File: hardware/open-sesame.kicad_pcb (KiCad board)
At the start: 2 copper layers, 72.2 x 45 mm, 9 parts, among them J1 Conn_01x10, J3 Barrel_Jack_Switch, J4 Conn_01x06_Socket

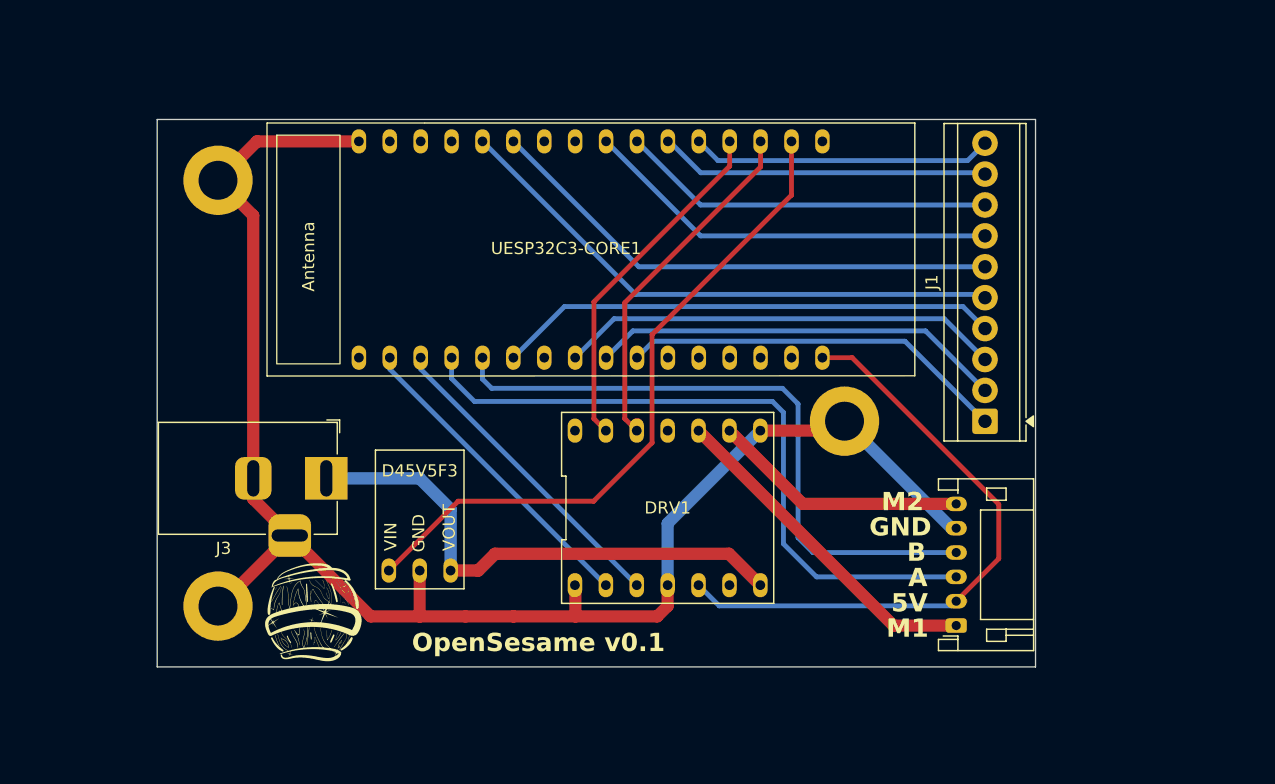
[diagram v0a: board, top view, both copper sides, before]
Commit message: Updated 3V & GND to terminal block
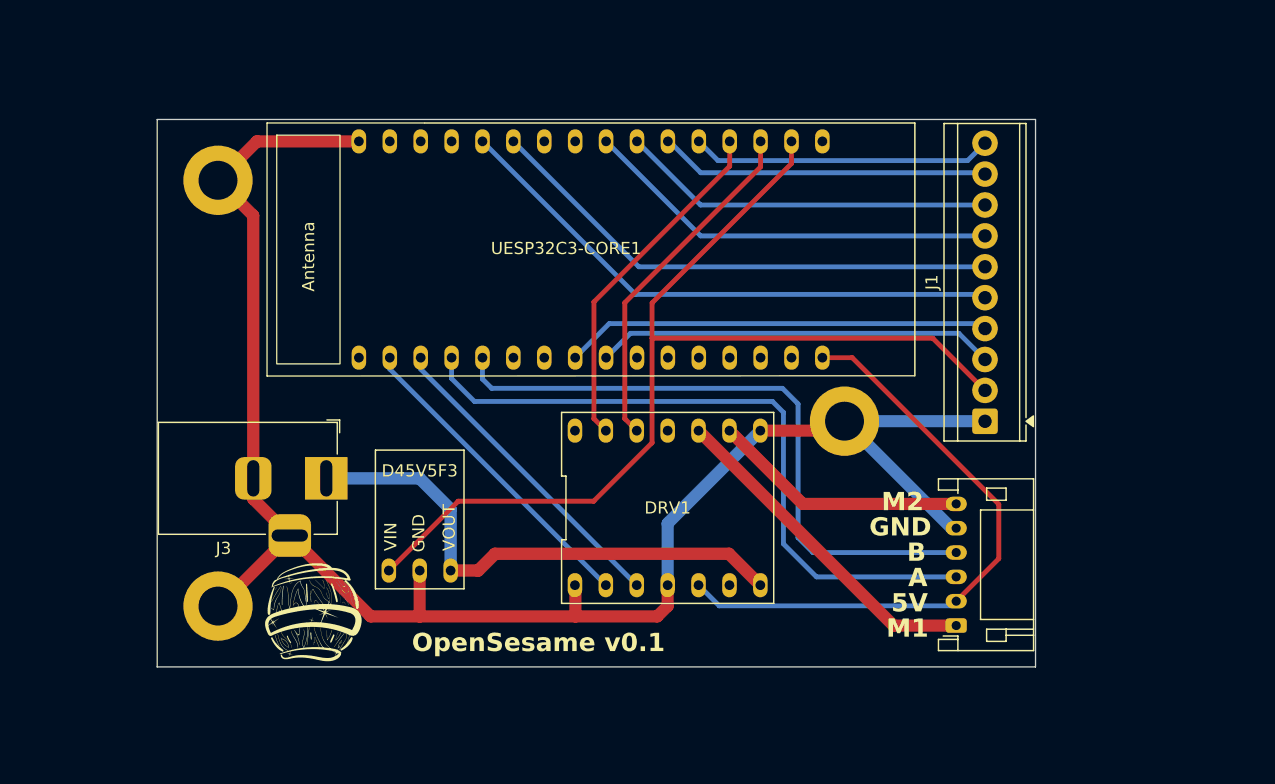
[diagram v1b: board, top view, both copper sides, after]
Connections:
- J1 pad 1: Net-(J1-Pin_1) -> GND
- J1 pad 2: Net-(J1-Pin_2) -> +3V3
- UESP32C3-CORE1 pad 10: Net-(J1-Pin_1) -> unconnected-(UESP32C3-CORE1-GPIO13-Pad10)
- UESP32C3-CORE1 pad 6: Net-(J1-Pin_4) -> unconnected-(UESP32C3-CORE1-GPIO19-Pad6)
- UESP32C3-CORE1 pad 8: Net-(J1-Pin_3) -> Net-(J1-Pin_4)
- UESP32C3-CORE1 pad 9: Net-(J1-Pin_2) -> Net-(J1-Pin_3)
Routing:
- net Net-(J1-Pin_2): track 34.1 -> 0.00 mm
- net Net-(J1-Pin_1): track 31.9 -> 0.00 mm
- net +3V3: track 55.5 -> 84.7 mm
- net GND: track 131.0 -> 141.3 mm
- net Net-(J1-Pin_4): track 41.3 -> 34.4 mm
- net Net-(J1-Pin_3): track 36.4 -> 32.9 mm
- net +5V: track 51.7 -> 50.4 mm
- net FAULT: track 29.7 -> 28.8 mm
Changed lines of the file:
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@@
 	(net 15 "unconnected-(UESP32C3-CORE1-GPIO08-Pad29)")
 	(net 16 "Net-(J1-Pin_8)")
-	(net 17 "Net-(J1-Pin_1)")
+	(net 17 "unconnected-(UESP32C3-CORE1-GPIO19-Pad6)")
 	(net 18 "unconnected-(UESP32C3-CORE1-REST-Pad12)")
 	(net 19 "unconnected-(UESP32C3-CORE1-GPIO09{slash}BOOT-Pad30)")
-	(net 20 "Net-(J1-Pin_2)")
+	(net 20 "unconnected-(UESP32C3-CORE1-GPIO13-Pad10)")
 	(net 21 "Net-(J1-Pin_4)")
 	(net 22 "A")
@@
 			(remove_unused_layers no)
 			(roundrect_rratio 0.119048)
-			(net 17 "Net-(J1-Pin_1)")
+			(net 2 "GND")
 			(pinfunction "Pin_1")
 			(pintype "passive")
@@
 			(layers "*.Cu" "*.Mask")
 			(remove_unused_layers no)
-			(net 20 "Net-(J1-Pin_2)")
+			(net 1 "+3V3")
 			(pinfunction "Pin_2")
 			(pintype "passive")
@@
 				(font
 					(size 1 1)
-					(thickness 0.1)
+					(thickness 0.127)
 				)
 				(justify left bottom)
@@
 			(layers "*.Cu" "*.Mask")
 			(remove_unused_layers no)
-			(net 21 "Net-(J1-Pin_4)")
+			(net 17 "unconnected-(UESP32C3-CORE1-GPIO19-Pad6)")
 			(pinfunction "GPIO19")
-			(pintype "bidirectional")
+			(pintype "bidirectional+no_connect")
 			(thermal_bridge_angle 45)
 		)
@@
 			(layers "*.Cu" "*.Mask")
 			(remove_unused_layers no)
-			(net 12 "Net-(J1-Pin_3)")
+			(net 21 "Net-(J1-Pin_4)")
 			(pinfunction "UART0_RX")
 			(pintype "input")
@@
 			(layers "*.Cu" "*.Mask")
 			(remove_unused_layers no)
-			(net 20 "Net-(J1-Pin_2)")
+			(net 12 "Net-(J1-Pin_3)")
 			(pinfunction "UART0_TX")
 			(pintype "output")
@@
 			(layers "*.Cu" "*.Mask")
 			(remove_unused_layers no)
-			(net 17 "Net-(J1-Pin_1)")
+			(net 20 "unconnected-(UESP32C3-CORE1-GPIO13-Pad10)")
 			(pinfunction "GPIO13")
-			(pintype "bidirectional")
+			(pintype "bidirectional+no_connect")
 			(thermal_bridge_angle 45)
 		)
@@
 				(font
 					(size 1 1)
-					(thickness 0.1)
+					(thickness 0.127)
 				)
 				(justify left bottom)
@@
 				(font
 					(size 1 1)
-					(thickness 0.1)
+					(thickness 0.127)
 				)
 				(justify left bottom)
@@
 				(font
 					(size 1 1)
-					(thickness 0.1)
+					(thickness 0.127)
 				)
 				(justify left bottom)
@@
 	)
 	(segment
-		(start 139.86 104.7)
-		(end 145.56 99)
+		(start 145.56 99)
+		(end 156.7 99)
 		(width 0.4)
 		(layer "F.Cu")
@@
 	)
 	(segment
-		(start 145.56 99)
-		(end 156.7 99)
+		(start 184.5775 85.6)
+		(end 188.8675 89.89)
 		(width 0.4)
 		(layer "F.Cu")
@@
 	)
 	(segment
-		(start 172.96 73.84)
-		(end 172.96 69.42)
+		(start 161.5 82.7)
+		(end 172.96 71.24)
 		(width 0.4)
 		(layer "F.Cu")
@@
 	)
 	(segment
-		(start 156.7 99)
-		(end 161.5 94.2)
+		(start 161.5 85.6)
+		(end 161.5 82.7)
 		(width 0.4)
 		(layer "F.Cu")
@@
 	)
 	(segment
-		(start 161.5 85.3)
-		(end 172.96 73.84)
+		(start 161.5 94.2)
+		(end 161.5 85.6)
 		(width 0.4)
 		(layer "F.Cu")
@@
 	)
 	(segment
-		(start 161.5 94.2)
-		(end 161.5 85.3)
+		(start 156.7 99)
+		(end 161.5 94.2)
 		(width 0.4)
 		(layer "F.Cu")
@@
 	)
 	(segment
-		(start 155.2 105.94)
-		(end 155.16 105.9)
-		(width 1)
+		(start 172.96 71.24)
+		(end 172.96 69.42)
+		(width 0.4)
 		(layer "F.Cu")
-		(net 2)
+		(net 1)
 	)
 	(segment
-		(start 161.93 108.47)
-		(end 162.78 107.62)
-		(width 1)
+		(start 161.5 85.6)
+		(end 184.5775 85.6)
+		(width 0.4)
 		(layer "F.Cu")
-		(net 2)
+		(net 1)
 	)
 	(segment
-		(start 146.17 108.47)
-		(end 142.4 108.47)
-		(width 1)
+		(start 139.86 104.7)
+		(end 145.56 99)
+		(width 0.4)
 		(layer "F.Cu")
-		(net 2)
+		(net 1)
 	)
 	(segment
-		(start 125.82 107.62)
-		(end 125.92 107.62)
+		(start 161.93 108.47)
+		(end 162.78 107.62)
 		(width 1)
 		(layer "F.Cu")
@@
 	)
 	(segment
-		(start 150.1 108.47)
-		(end 155.2 108.47)
-		(width 1)
-		(layer "F.Cu")
-		(net 2)
-	)
-	(segment
 		(start 170.4 93.2)
 		(end 176.54 93.2)
@@
 	)
 	(segment
-		(start 176.54 93.2)
-		(end 177.32 92.42)
-		(width 1)
-		(layer "F.Cu")
-		(net 2)
-	)
-	(segment
 		(start 142.4 108.47)
 		(end 138.37 108.47)
@@
 	)
 	(segment
-		(start 150.1 108.47)
-		(end 146.17 108.47)
+		(start 142.4 108.47)
+		(end 155.2 108.47)
 		(width 1)
 		(layer "F.Cu")
@@
 	)
 	(segment
-		(start 150.1 108.47)
-		(end 150.12 108.45)
-		(width 1)
-		(layer "F.Cu")
-		(net 2)
-	)
-	(segment
 		(start 186.5 101.22)
 		(end 186.12 101.22)
@@
 	)
 	(segment
+		(start 177.32 92.42)
+		(end 188.8575 92.42)
+		(width 1)
+		(layer "B.Cu")
+		(net 2)
+	)
+	(segment
 		(start 144.94 104.7)
 		(end 147.21 104.7)
@@
 	)
 	(segment
-		(start 187.22 107.22)
-		(end 186.5 107.22)
-		(width 0.4)
-		(layer "F.Cu")
-		(net 8)
-	)
-	(segment
 		(start 177.95 87.2)
 		(end 190 99.25)
@@
 	)
 	(segment
-		(start 186.12 107.6)
-		(end 186.5 107.22)
-		(width 0.4)
-		(layer "B.Cu")
-		(net 8)
-	)
-	(segment
 		(start 165.32 105.9)
 		(end 167.02 107.6)
@@
 	)
 	(segment
-		(start 158.38 84)
-		(end 185.5175 84)
+		(start 186.7175 85.2)
+		(end 159.72 85.2)
 		(width 0.4)
 		(layer "B.Cu")
@@
 	)
 	(segment
-		(start 185.5175 84)
-		(end 188.8675 87.35)
+		(start 159.72 85.2)
+		(end 157.72 87.2)
 		(width 0.4)
 		(layer "B.Cu")
@@
 	)
 	(segment
-		(start 155.18 87.2)
-		(end 158.38 84)
+		(start 188.8675 87.35)
+		(end 186.7175 85.2)
 		(width 0.4)
 		(layer "B.Cu")
@@
 	)
 	(segment
-		(start 188.8675 82.27)
-		(end 188.5975 82)
-		(width 0.4)
-		(layer "B.Cu")
-		(net 14)
-	)
-	(segment
 		(start 188.8675 74.65)
 		(end 165.49 74.65)
@@
 	)
 	(segment
-		(start 182.2865 85.849)
-		(end 188.8675 92.43)
-		(width 0.4)
-		(layer "B.Cu")
-		(net 17)
-	)
-	(segment
-		(start 161.611 85.849)
-		(end 182.2865 85.849)
-		(width 0.4)
-		(layer "B.Cu")
-		(net 17)
-	)
-	(segment
-		(start 160.26 87.2)
-		(end 161.611 85.849)
-		(width 0.4)
-		(layer "B.Cu")
-		(net 17)
-	)
-	(segment
-		(start 159.92 85)
-		(end 183.9775 85)
-		(width 0.4)
-		(layer "B.Cu")
-		(net 20)
-	)
-	(segment
-		(start 183.9775 85)
-		(end 188.8675 89.89)
-		(width 0.4)
-		(layer "B.Cu")
-		(net 20)
-	)
-	(segment
-		(start 157.72 87.2)
-		(end 159.92 85)
-		(width 0.4)
-		(layer "B.Cu")
-		(net 20)
-	)
-	(segment
-		(start 150.1 87.2)
-		(end 154.3 83)
+		(start 157.98 84.4)
+		(end 155.18 87.2)
 		(width 0.4)
 		(layer "B.Cu")
@@
 	)
 	(segment
-		(start 154.3 83)
-		(end 187.0575 83)
-		(width 0.4)
-		(layer "B.Cu")
-		(net 21)
-	)
-	(segment
-		(start 187.0575 83)
-		(end 188.8675 84.81)
+		(start 188.4575 84.4)
+		(end 157.98 84.4)
 		(width 0.4)
 		(layer "B.Cu")
@@
 	)
 	(segment
-		(start 160.28 92.66)
-		(end 160.28 93.52)
-		(width 1)
-		(layer "F.Cu")
-		(net 24)
-	)
-	(segment
 		(start 159.259 92.219)
 		(end 160.24 93.2)
@@
 	)
 	(segment
-		(start 162.92 69.42)
-		(end 162.8 69.42)
-		(width 0.4)
-		(layer "B.Cu")
-		(net 26)
-	)
-	(segment
 		(start 165.5 72)
 		(end 162.92 69.42)
 		(width 0.4)
 		(layer "B.Cu")
-		(net 26)
-	)
-	(segment
-		(start 188.8675 72.11)
-		(end 188.7575 72)
-		(width 0.4)
-		(layer "B.Cu")

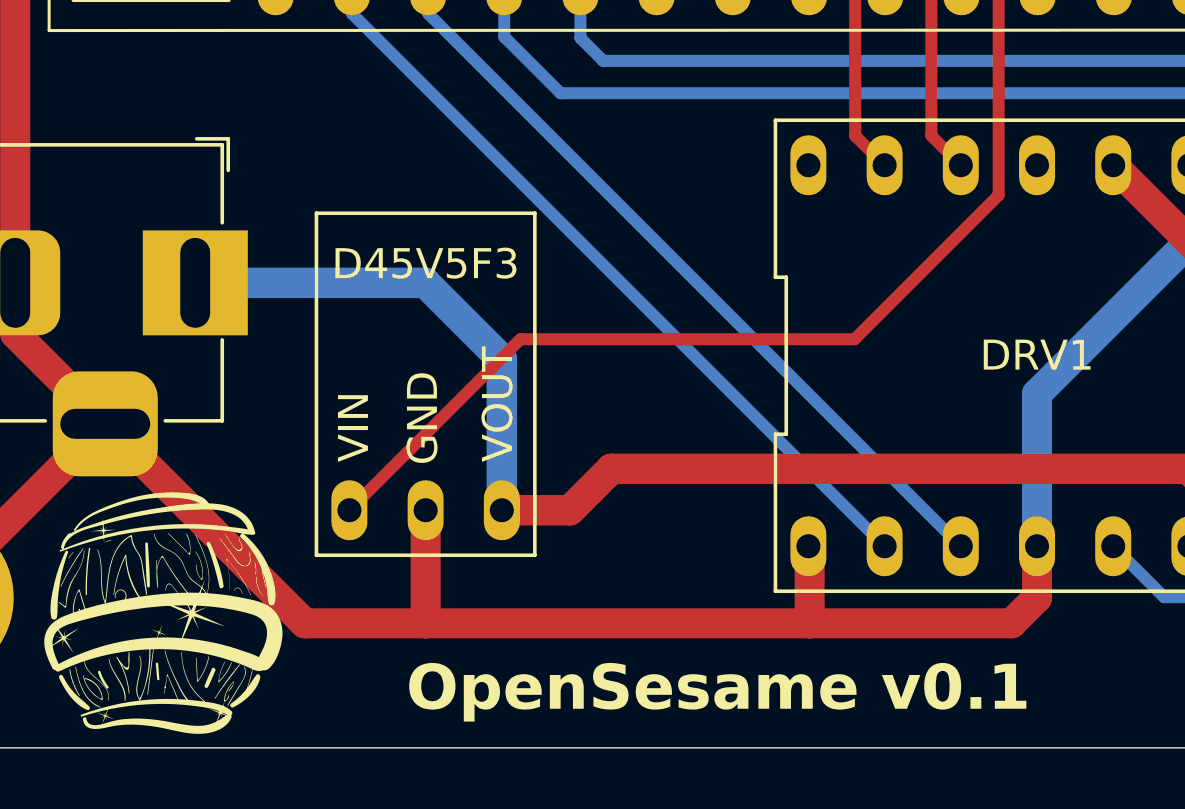
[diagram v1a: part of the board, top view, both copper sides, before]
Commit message: fix(hardware): Corrected VIN&VOUT
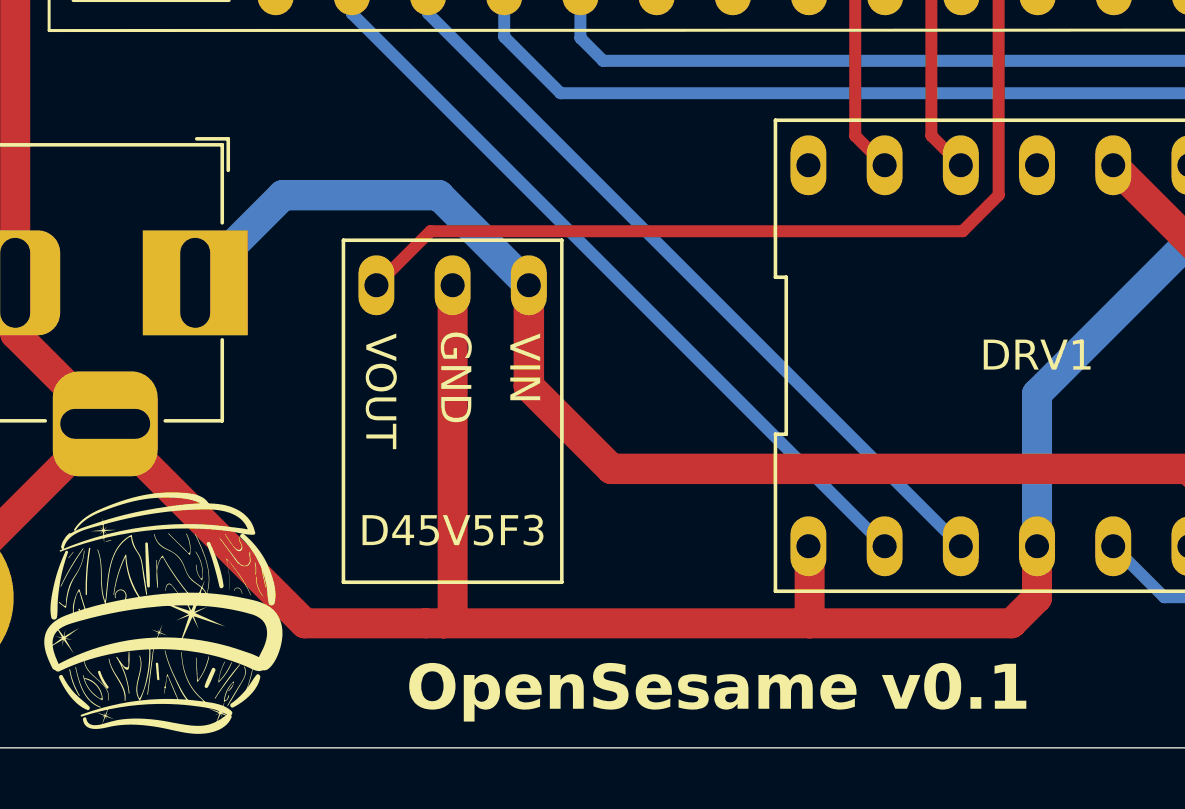
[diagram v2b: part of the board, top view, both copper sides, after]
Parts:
- moved D45V5F3 7.55 mm to (143.3, 97.2), turned to 180 degrees
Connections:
- D45V5F3 pad 1: +3V3 -> +24V
- D45V5F3 pad 3: +24V -> +3V3
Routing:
- net GND: track 141.3 -> 148.9 mm
- net +3V3: track 84.7 -> 80.7 mm
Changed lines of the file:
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@@
 		)
 		(property "Value" "MountingHole_Pad"
-			(at 0 3.8 0)
+			(at -1.32 4.18 0)
 			(layer "F.Fab")
 			(effects
@@
 		(property ki_fp_filters "MountingHole*Pad*")
 		(sheetname "/")
-		(sheetfile "ferrous-oxslide2.kicad_sch")
+		(sheetfile "open-sesame.kicad_sch")
 		(attr exclude_from_pos_files exclude_from_bom)
 		(fp_circle
@@
 		(property ki_fp_filters "Connector*:*_1x??_*")
 		(sheetname "/")
-		(sheetfile "ferrous-oxslide2.kicad_sch")
+		(sheetfile "open-sesame.kicad_sch")
 		(attr through_hole)
 		(fp_line
@@
 		)
 		(sheetname "/")
-		(sheetfile "ferrous-oxslide2.kicad_sch")
+		(sheetfile "open-sesame.kicad_sch")
 		(attr through_hole)
 		(fp_line
@@
 		(property ki_fp_filters "BarrelJack*")
 		(sheetname "/")
-		(sheetfile "ferrous-oxslide2.kicad_sch")
+		(sheetfile "open-sesame.kicad_sch")
 		(attr through_hole)
 		(fp_line
@@
 		(property ki_fp_filters "Connector*:*_1x??_*")
 		(sheetname "/")
-		(sheetfile "ferrous-oxslide2.kicad_sch")
+		(sheetfile "open-sesame.kicad_sch")
 		(attr through_hole)
 		(fp_line
@@
 		(property ki_fp_filters "MountingHole*Pad*")
 		(sheetname "/")
-		(sheetfile "ferrous-oxslide2.kicad_sch")
+		(sheetfile "open-sesame.kicad_sch")
 		(attr exclude_from_pos_files exclude_from_bom)
 		(fp_circle
@@
 		(property ki_fp_filters "MountingHole*Pad*")
 		(sheetname "/")
-		(sheetfile "ferrous-oxslide2.kicad_sch")
+		(sheetfile "open-sesame.kicad_sch")
 		(attr exclude_from_pos_files exclude_from_bom)
 		(fp_circle
@@
 	(footprint "Library:D45V5Fx"
 		(layer "F.Cu")
-		(at 142.4 104.7)
+		(at 143.3 97.2 180)
 		(property "Reference" "D45V5F3"
 			(at 0 -8.2 0)
@@
 		)
 		(sheetname "/")
-		(sheetfile "ferrous-oxslide2.kicad_sch")
+		(sheetfile "open-sesame.kicad_sch")
 		(attr through_hole)
 		(fp_line
-			(start -3.64 1.5)
-			(end -3.64 -9.9)
+			(start 3.64 1.5)
+			(end -3.64 1.5)
 			(stroke
 				(width 0.12)
@@
 		(fp_line
 			(start 3.64 -9.9)
-			(end -3.64 -9.9)
+			(end 3.64 1.5)
 			(stroke
 				(width 0.12)
@@
 		(fp_line
 			(start 3.64 -9.9)
-			(end 3.64 1.5)
+			(end -3.64 -9.9)
 			(stroke
 				(width 0.12)
@@
 		)
 		(fp_line
-			(start 3.64 1.5)
-			(end -3.64 1.5)
+			(start -3.64 1.5)
+			(end -3.64 -9.9)
 			(stroke
 				(width 0.12)
@@
 		)
 		(fp_line
-			(start -3.39 -1.25)
-			(end 3.39 -1.25)
+			(start 3.39 1.25)
+			(end -3.39 1.25)
 			(stroke
 				(width 0.05)
@@
 		)
 		(fp_line
-			(start -3.39 1.25)
-			(end -3.39 -1.25)
+			(start 3.39 -1.25)
+			(end 3.39 1.25)
 			(stroke
 				(width 0.05)
@@
 		)
 		(fp_line
-			(start 3.39 -1.25)
-			(end 3.39 1.25)
+			(start -3.39 1.25)
+			(end -3.39 -1.25)
 			(stroke
 				(width 0.05)
@@
 		)
 		(fp_line
-			(start 3.39 1.25)
-			(end -3.39 1.25)
+			(start -3.39 -1.25)
+			(end 3.39 -1.25)
 			(stroke
 				(width 0.05)
@@
 		)
 		(fp_text user "GND"
-			(at 0.5 -1.5 90)
+			(at 0.5 -1.5 270)
 			(unlocked yes)
 			(layer "F.SilkS")
@@
 		)
 		(fp_text user "VIN"
-			(at -1.8 -1.6 90)
+			(at -1.8 -1.6 270)
 			(unlocked yes)
 			(layer "F.SilkS")
@@
 		)
 		(fp_text user "VOUT"
-			(at 3 -1.6 90)
+			(at 3 -1.6 270)
 			(unlocked yes)
 			(layer "F.SilkS")
@@
 		)
 		(pad "1" thru_hole oval
-			(at -2.54 0)
+			(at -2.54 0 180)
 			(size 1.2 2)
 			(drill 0.8)
 			(layers "*.Cu" "*.Mask")
 			(remove_unused_layers no)
-			(net 1 "+3V3")
+			(net 3 "+24V")
 			(pinfunction "VOUT")
 			(pintype "power_out")
@@
 		)
 		(pad "2" thru_hole oval
-			(at 0 0)
+			(at 0 0 180)
 			(size 1.2 2)
 			(drill 0.8)
@@
 		)
 		(pad "3" thru_hole oval
-			(at 2.54 0)
+			(at 2.54 0 180)
 			(size 1.2 2)
 			(drill 0.8)
 			(layers "*.Cu" "*.Mask")
 			(remove_unused_layers no)
-			(net 3 "+24V")
+			(net 1 "+3V3")
 			(pinfunction "VIN")
 			(pintype "power_in")
@@
 		)
 		(sheetname "/")
-		(sheetfile "ferrous-oxslide2.kicad_sch")
+		(sheetfile "open-sesame.kicad_sch")
 		(attr through_hole)
 		(fp_line
@@
 	)
 	(segment
-		(start 145.56 99)
-		(end 156.7 99)
+		(start 161.5 94.2)
+		(end 161.5 85.6)
 		(width 0.4)
 		(layer "F.Cu")
@@
 	)
 	(segment
-		(start 161.5 82.7)
-		(end 172.96 71.24)
+		(start 160.3 95.4)
+		(end 161.5 94.2)
 		(width 0.4)
 		(layer "F.Cu")
@@
 	)
 	(segment
-		(start 161.5 85.6)
-		(end 161.5 82.7)
+		(start 140.76 97.2)
+		(end 142.56 95.4)
 		(width 0.4)
 		(layer "F.Cu")
@@
 	)
 	(segment
-		(start 161.5 94.2)
-		(end 161.5 85.6)
+		(start 161.5 82.7)
+		(end 172.96 71.24)
 		(width 0.4)
 		(layer "F.Cu")
@@
 	)
 	(segment
-		(start 156.7 99)
-		(end 161.5 94.2)
+		(start 161.5 85.6)
+		(end 161.5 82.7)
 		(width 0.4)
 		(layer "F.Cu")
@@
 	)
 	(segment
-		(start 139.86 104.7)
-		(end 145.56 99)
+		(start 142.56 95.4)
+		(end 160.3 95.4)
 		(width 0.4)
 		(layer "F.Cu")
@@
 	(segment
 		(start 142.4 108.47)
-		(end 155.2 108.47)
+		(end 143 108.47)
 		(width 1)
 		(layer "F.Cu")
@@
 	)
 	(segment
-		(start 128.72 75.52)
-		(end 128.72 97.12)
+		(start 143 108.47)
+		(end 155.2 108.47)
 		(width 1)
 		(layer "F.Cu")
@@
 	)
 	(segment
-		(start 142.4 108.47)
-		(end 142.4 104.7)
+		(start 128.72 75.52)
+		(end 128.72 97.12)
 		(width 1)
 		(layer "F.Cu")
@@
 	)
 	(segment
+		(start 143.3 108.17)
+		(end 143.3 97.2)
+		(width 1)
+		(layer "F.Cu")
+		(net 2)
+	)
+	(segment
 		(start 125.92 107.62)
 		(end 131.72 101.82)
@@
 	)
 	(segment
+		(start 143 108.47)
+		(end 143.3 108.17)
+		(width 1)
+		(layer "F.Cu")
+		(net 2)
+	)
+	(segment
 		(start 125.82 72.62)
 		(end 128.72 75.52)
@@
 	)
 	(segment
-		(start 144.94 104.7)
-		(end 147.21 104.7)
+		(start 145.84 100.57)
+		(end 145.84 97.2)
 		(width 1.016)
 		(layer "F.Cu")
@@
 	(segment
 		(start 148.59 103.32)
-		(end 167.82 103.32)
+		(end 145.84 100.57)
 		(width 1.016)
 		(layer "F.Cu")
@@
 	)
 	(segment
-		(start 147.21 104.7)
-		(end 148.59 103.32)
+		(start 148.59 103.32)
+		(end 167.82 103.32)
 		(width 1.016)
 		(layer "F.Cu")
@@
 	)
 	(segment
-		(start 142.39 97.12)
-		(end 134.72 97.12)
+		(start 134.72 97.12)
+		(end 137.64 94.2)
 		(width 1.016)
 		(layer "B.Cu")
@@
 	)
 	(segment
-		(start 142.39 97.12)
-		(end 144.94 99.67)
+		(start 142.84 94.2)
+		(end 145.84 97.2)
 		(width 1.016)
 		(layer "B.Cu")
@@
 	)
 	(segment
-		(start 144.94 99.67)
-		(end 144.94 104.7)
+		(start 137.64 94.2)
+		(end 142.84 94.2)
 		(width 1.016)
 		(layer "B.Cu")
